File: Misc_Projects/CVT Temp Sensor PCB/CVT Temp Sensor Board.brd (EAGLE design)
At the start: 160 x 100 mm, 2 parts, among them IC1 TSD305-1SL10

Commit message: CVT Temp Board Sensor PCB
Version 1.1
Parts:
- moved IC1 27.2 mm to (99.6, 33.0)
- moved X1 24.3 mm to (81.4, 33.3), turned to 270 degrees
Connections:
- removed net N$2: X1.P$2
- removed net N$3: X1.P$3
- new net SCL: IC1.1, X1.P$3
- new net SDA: IC1.2, X1.P$2
- net +3V3: now also IC1.3
- net GND: now also IC1.4
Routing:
- net GND: track 0.00 -> 18.7 mm
- net SDA: track 0.00 -> 11.8 mm
- net SCL: track 0.00 -> 11.4 mm
- net +3V3: track 0.00 -> 9.28 mm
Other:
- board size 160 x 100 mm -> 26.9 x 24.8 mm
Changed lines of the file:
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@@
 <setting verticaltext="up"/>
 </settings>
-<grid distance="50" unitdist="mil" unit="mil" style="lines" multiple="1" display="no" altdistance="5" altunitdist="mil" altunit="mil"/>
+<grid distance="5" unitdist="mil" unit="mil" style="lines" multiple="1" display="yes" altdistance="5" altunitdist="mil" altunit="mil"/>
 <layers>
 <layer number="1" name="Top" color="4" fill="1" visible="yes" active="yes"/>
@@
 <board>
 <plain>
-<wire x1="0" y1="0" x2="160" y2="0" width="0" layer="20"/>
-<wire x1="160" y1="0" x2="160" y2="100" width="0" layer="20"/>
-<wire x1="160" y1="100" x2="0" y2="100" width="0" layer="20"/>
-<wire x1="0" y1="100" x2="0" y2="0" width="0" layer="20"/>
+<wire x1="78.867" y1="20.828" x2="105.771" y2="20.828" width="0" layer="20"/>
+<wire x1="105.771" y1="20.828" x2="105.771" y2="45.644" width="0" layer="20"/>
+<wire x1="105.771" y1="45.644" x2="78.867" y2="45.644" width="0" layer="20"/>
+<wire x1="78.867" y1="45.644" x2="78.867" y2="20.828" width="0" layer="20"/>
 </plain>
 <attributes>
@@
 </autorouter>
 <elements>
-<element name="IC1" library="TSD305-1SL10" package="TSD3051SL10" value="TSD305-1SL10" x="72.39" y="33.02" smashed="yes">
-<attribute name="DESCRIPTION" value="Board Mount Temperature Sensors TO5, I2C Interrface 0 C to +300 C" x="90.17" y="26.67" size="1.778" layer="27" display="off"/>
-<attribute name="HEIGHT" value="8.65mm" x="90.17" y="26.67" size="1.778" layer="27" display="off"/>
-<attribute name="MANUFACTURER_NAME" value="TE Connectivity" x="90.17" y="26.67" size="1.778" layer="27" display="off"/>
-<attribute name="MANUFACTURER_PART_NUMBER" value="TSD305-1SL10" x="90.17" y="26.67" size="1.778" layer="27" display="off"/>
-<attribute name="MOUSER_PART_NUMBER" value="824-TSD305-1SL10" x="90.17" y="26.67" size="1.778" layer="27" display="off"/>
-<attribute name="MOUSER_PRICE-STOCK" value="https://www.mouser.co.uk/ProductDetail/Measurement-Specialties/TSD305-1SL10?qs=l7cgNqFNU1hQbECGfV0ZYg%3D%3D" x="90.17" y="26.67" size="1.778" layer="27" display="off"/>
-<attribute name="NAME" x="69.85" y="33.02" size="1.27" layer="25" align="center"/>
-<attribute name="VALUE" x="69.85" y="40.64" size="1.27" layer="27" align="center"/>
+<element name="IC1" library="TSD305-1SL10" package="TSD3051SL10" value="TSD305-1SL10" x="99.568" y="33.02" smashed="yes">
+<attribute name="DESCRIPTION" value="Board Mount Temperature Sensors TO5, I2C Interrface 0 C to +300 C" x="117.348" y="26.67" size="1.778" layer="27" display="off"/>
+<attribute name="HEIGHT" value="8.65mm" x="117.348" y="26.67" size="1.778" layer="27" display="off"/>
+<attribute name="MANUFACTURER_NAME" value="TE Connectivity" x="117.348" y="26.67" size="1.778" layer="27" display="off"/>
+<attribute name="MANUFACTURER_PART_NUMBER" value="TSD305-1SL10" x="117.348" y="26.67" size="1.778" layer="27" display="off"/>
+<attribute name="MOUSER_PART_NUMBER" value="824-TSD305-1SL10" x="117.348" y="26.67" size="1.778" layer="27" display="off"/>
+<attribute name="MOUSER_PRICE-STOCK" value="https://www.mouser.co.uk/ProductDetail/Measurement-Specialties/TSD305-1SL10?qs=l7cgNqFNU1hQbECGfV0ZYg%3D%3D" x="117.348" y="26.67" size="1.778" layer="27" display="off"/>
+<attribute name="NAME" x="97.028" y="33.02" size="1.27" layer="25" rot="R180" align="center"/>
+<attribute name="VALUE" x="97.409" y="40.005" size="1.27" layer="27" align="center"/>
 </element>
-<element name="X1" library="GTOR - Microfit Connector" package="43045-0400" value="" x="57.15" y="33.02" smashed="yes">
-<attribute name="MATERIAL" value="" x="57.15" y="33.02" size="1.778" layer="27" display="off"/>
+<element name="X1" library="GTOR - Microfit Connector" package="43045-0400" value="" x="81.407" y="33.274" smashed="yes" rot="R270">
+<attribute name="MATERIAL" value="" x="81.407" y="33.274" size="1.778" layer="27" rot="R270" display="off"/>
 </element>
 </elements>
@@
 <signal name="+3V3">
 <contactref element="X1" pad="P$1"/>
+<contactref element="IC1" pad="3"/>
+<wire x1="85.727" y1="31.774" x2="87.32183125" y2="31.774" width="0.1524" layer="1"/>
+<wire x1="87.32183125" y1="31.774" x2="88.31543125" y2="32.7676" width="0.1524" layer="1"/>
+<wire x1="94.2356" y1="32.7676" x2="94.488" y2="33.02" width="0.1524" layer="1"/>
+<wire x1="88.31543125" y1="32.7676" x2="94.2356" y2="32.7676" width="0.1524" layer="1"/>
 </signal>
-<signal name="N$2">
+<signal name="SDA">
 <contactref element="X1" pad="P$2"/>
+<contactref element="IC1" pad="2"/>
+<wire x1="85.727" y1="34.774" x2="86.767" y2="35.814" width="0.1524" layer="1"/>
+<wire x1="96.774" y1="35.814" x2="86.767" y2="35.814" width="0.1524" layer="1"/>
+<wire x1="96.774" y1="35.814" x2="97.028" y2="35.56" width="0.1524" layer="1"/>
 </signal>
-<signal name="N$3">
+<signal name="SCL">
 <contactref element="X1" pad="P$3"/>
+<contactref element="IC1" pad="1"/>
+<wire x1="88.727" y1="31.774" x2="98.322" y2="31.774" width="0.1524" layer="1"/>
+<wire x1="98.322" y1="31.774" x2="99.568" y2="33.02" width="0.1524" layer="1"/>
 </signal>
 <signal name="GND">
 <contactref element="X1" pad="P$4"/>
+<contactref element="IC1" pad="4"/>
+<wire x1="88.727" y1="34.774" x2="99.465" y2="34.774" width="0.1524" layer="1"/>
+<wire x1="99.465" y1="34.774" x2="101.092" y2="33.147" width="0.1524" layer="1"/>
+<wire x1="101.092" y1="33.147" x2="101.092" y2="32.258" width="0.1524" layer="1"/>
+<wire x1="101.092" y1="32.258" x2="99.314" y2="30.48" width="0.1524" layer="1"/>
+<wire x1="99.314" y1="30.48" x2="97.028" y2="30.48" width="0.1524" layer="1"/>
 </signal>
 </signals>

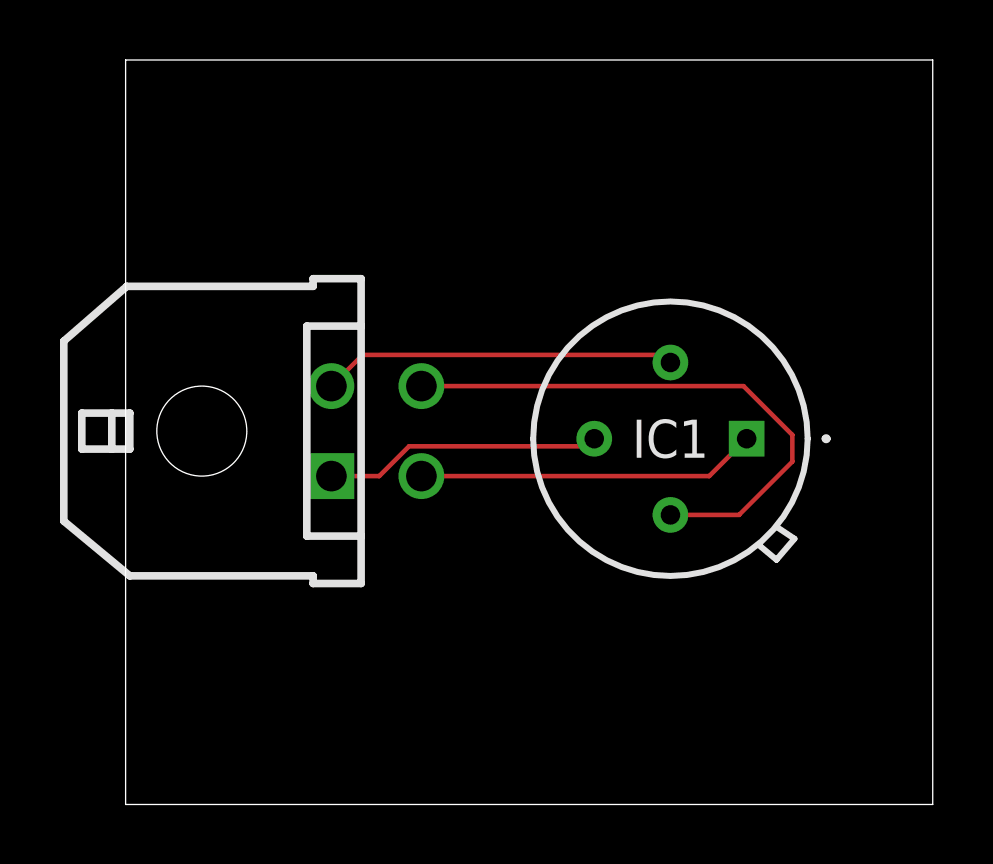
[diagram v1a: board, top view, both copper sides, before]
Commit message: added designer names
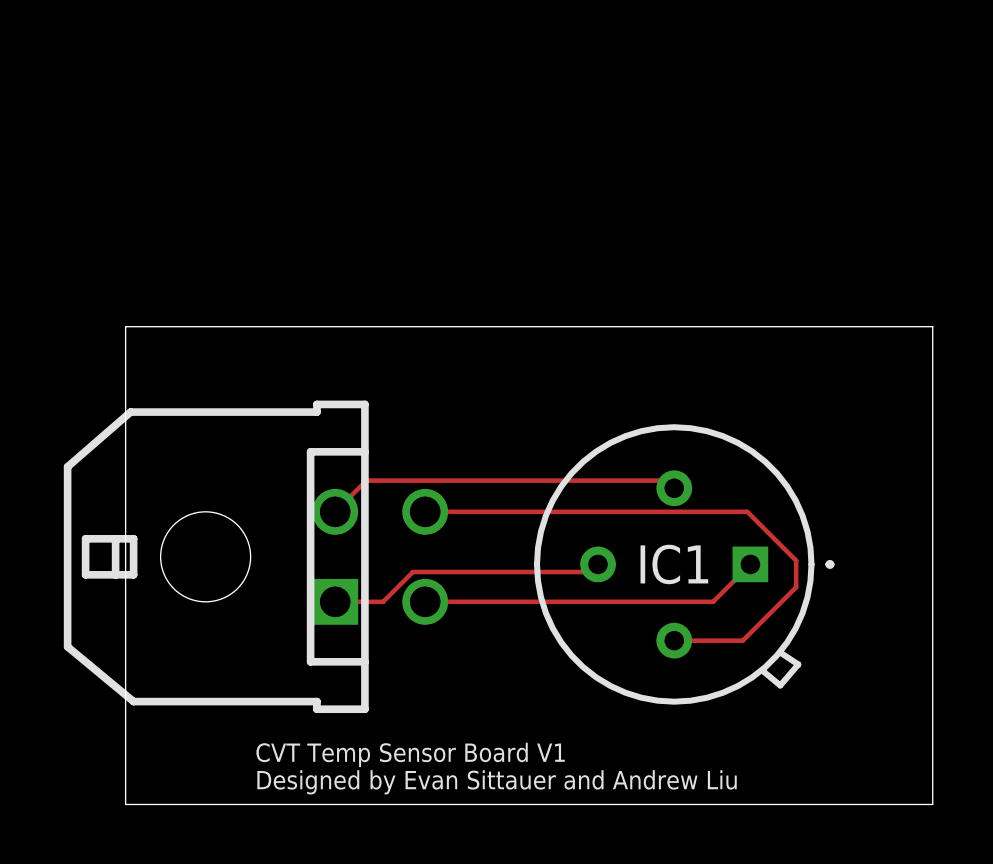
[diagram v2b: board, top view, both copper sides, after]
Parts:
- moved X1 4.19 mm to (81.5, 29.1)
- moved IC1 4.19 mm to (99.7, 28.8)
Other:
- board size 26.9 x 24.8 mm -> 26.9 x 15.9 mm
- board text added: "CVT Temp Sensor Board V1 Designed by Evan Sittauer and Andrew Liu"
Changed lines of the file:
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@@
 <layer number="43" name="vRestrict" color="2" fill="10" visible="yes" active="yes"/>
 <layer number="44" name="Drills" color="7" fill="1" visible="no" active="yes"/>
-<layer number="45" name="Holes" color="7" fill="1" visible="no" active="yes"/>
+<layer number="45" name="Holes" color="7" fill="1" visible="yes" active="yes"/>
 <layer number="46" name="Milling" color="3" fill="1" visible="no" active="yes"/>
 <layer number="47" name="Measures" color="7" fill="1" visible="no" active="yes"/>
@@
 <plain>
 <wire x1="78.867" y1="20.828" x2="105.771" y2="20.828" width="0" layer="20"/>
-<wire x1="105.771" y1="20.828" x2="105.771" y2="45.644" width="0" layer="20"/>
-<wire x1="105.771" y1="45.644" x2="78.867" y2="45.644" width="0" layer="20"/>
-<wire x1="78.867" y1="45.644" x2="78.867" y2="20.828" width="0" layer="20"/>
+<wire x1="105.771" y1="20.828" x2="105.771" y2="36.754" width="0" layer="20"/>
+<wire x1="105.771" y1="36.754" x2="78.867" y2="36.754" width="0" layer="20"/>
+<wire x1="78.867" y1="36.754" x2="78.867" y2="20.828" width="0" layer="20"/>
+<text x="83.185" y="21.336" size="0.6096" layer="25">CVT Temp Sensor Board V1
+Designed by Evan Sittauer and Andrew Liu</text>
 </plain>
 <attributes>
@@
 </autorouter>
 <elements>
-<element name="IC1" library="TSD305-1SL10" package="TSD3051SL10" value="TSD305-1SL10" x="99.568" y="33.02" smashed="yes">
-<attribute name="DESCRIPTION" value="Board Mount Temperature Sensors TO5, I2C Interrface 0 C to +300 C" x="117.348" y="26.67" size="1.778" layer="27" display="off"/>
-<attribute name="HEIGHT" value="8.65mm" x="117.348" y="26.67" size="1.778" layer="27" display="off"/>
-<attribute name="MANUFACTURER_NAME" value="TE Connectivity" x="117.348" y="26.67" size="1.778" layer="27" display="off"/>
-<attribute name="MANUFACTURER_PART_NUMBER" value="TSD305-1SL10" x="117.348" y="26.67" size="1.778" layer="27" display="off"/>
-<attribute name="MOUSER_PART_NUMBER" value="824-TSD305-1SL10" x="117.348" y="26.67" size="1.778" layer="27" display="off"/>
-<attribute name="MOUSER_PRICE-STOCK" value="https://www.mouser.co.uk/ProductDetail/Measurement-Specialties/TSD305-1SL10?qs=l7cgNqFNU1hQbECGfV0ZYg%3D%3D" x="117.348" y="26.67" size="1.778" layer="27" display="off"/>
-<attribute name="NAME" x="97.028" y="33.02" size="1.27" layer="25" rot="R180" align="center"/>
-<attribute name="VALUE" x="97.409" y="40.005" size="1.27" layer="27" align="center"/>
+<element name="IC1" library="TSD305-1SL10" package="TSD3051SL10" value="TSD305-1SL10" x="99.695" y="28.829" smashed="yes">
+<attribute name="DESCRIPTION" value="Board Mount Temperature Sensors TO5, I2C Interrface 0 C to +300 C" x="117.475" y="22.479" size="1.778" layer="27" display="off"/>
+<attribute name="HEIGHT" value="8.65mm" x="117.475" y="22.479" size="1.778" layer="27" display="off"/>
+<attribute name="MANUFACTURER_NAME" value="TE Connectivity" x="117.475" y="22.479" size="1.778" layer="27" display="off"/>
+<attribute name="MANUFACTURER_PART_NUMBER" value="TSD305-1SL10" x="117.475" y="22.479" size="1.778" layer="27" display="off"/>
+<attribute name="MOUSER_PART_NUMBER" value="824-TSD305-1SL10" x="117.475" y="22.479" size="1.778" layer="27" display="off"/>
+<attribute name="MOUSER_PRICE-STOCK" value="https://www.mouser.co.uk/ProductDetail/Measurement-Specialties/TSD305-1SL10?qs=l7cgNqFNU1hQbECGfV0ZYg%3D%3D" x="117.475" y="22.479" size="1.778" layer="27" display="off"/>
+<attribute name="NAME" x="97.155" y="28.829" size="1.27" layer="25" rot="R180" align="center"/>
+<attribute name="VALUE" x="97.536" y="35.814" size="1.27" layer="27" align="center"/>
 </element>
-<element name="X1" library="GTOR - Microfit Connector" package="43045-0400" value="" x="81.407" y="33.274" smashed="yes" rot="R270">
-<attribute name="MATERIAL" value="" x="81.407" y="33.274" size="1.778" layer="27" rot="R270" display="off"/>
+<element name="X1" library="GTOR - Microfit Connector" package="43045-0400" value="" x="81.534" y="29.083" smashed="yes" rot="R270">
+<attribute name="MATERIAL" value="" x="81.534" y="29.083" size="1.778" layer="27" rot="R270" display="off"/>
 </element>
 </elements>
@@
 <contactref element="X1" pad="P$1"/>
 <contactref element="IC1" pad="3"/>
-<wire x1="85.727" y1="31.774" x2="87.32183125" y2="31.774" width="0.1524" layer="1"/>
-<wire x1="87.32183125" y1="31.774" x2="88.31543125" y2="32.7676" width="0.1524" layer="1"/>
-<wire x1="94.2356" y1="32.7676" x2="94.488" y2="33.02" width="0.1524" layer="1"/>
-<wire x1="88.31543125" y1="32.7676" x2="94.2356" y2="32.7676" width="0.1524" layer="1"/>
+<wire x1="85.854" y1="27.583" x2="87.44883125" y2="27.583" width="0.1524" layer="1"/>
+<wire x1="87.44883125" y1="27.583" x2="88.44243125" y2="28.5766" width="0.1524" layer="1"/>
+<wire x1="94.3626" y1="28.5766" x2="94.615" y2="28.829" width="0.1524" layer="1"/>
+<wire x1="88.44243125" y1="28.5766" x2="94.3626" y2="28.5766" width="0.1524" layer="1"/>
 </signal>
 <signal name="SDA">
 <contactref element="X1" pad="P$2"/>
 <contactref element="IC1" pad="2"/>
-<wire x1="85.727" y1="34.774" x2="86.767" y2="35.814" width="0.1524" layer="1"/>
-<wire x1="96.774" y1="35.814" x2="86.767" y2="35.814" width="0.1524" layer="1"/>
-<wire x1="96.774" y1="35.814" x2="97.028" y2="35.56" width="0.1524" layer="1"/>
+<wire x1="85.854" y1="30.583" x2="86.894" y2="31.623" width="0.1524" layer="1"/>
+<wire x1="96.901" y1="31.623" x2="86.894" y2="31.623" width="0.1524" layer="1"/>
+<wire x1="96.901" y1="31.623" x2="97.155" y2="31.369" width="0.1524" layer="1"/>
 </signal>
 <signal name="SCL">
 <contactref element="X1" pad="P$3"/>
 <contactref element="IC1" pad="1"/>
-<wire x1="88.727" y1="31.774" x2="98.322" y2="31.774" width="0.1524" layer="1"/>
-<wire x1="98.322" y1="31.774" x2="99.568" y2="33.02" width="0.1524" layer="1"/>
+<wire x1="88.854" y1="27.583" x2="98.449" y2="27.583" width="0.1524" layer="1"/>
+<wire x1="98.449" y1="27.583" x2="99.695" y2="28.829" width="0.1524" layer="1"/>
 </signal>
 <signal name="GND">
 <contactref element="X1" pad="P$4"/>
 <contactref element="IC1" pad="4"/>
-<wire x1="88.727" y1="34.774" x2="99.465" y2="34.774" width="0.1524" layer="1"/>
-<wire x1="99.465" y1="34.774" x2="101.092" y2="33.147" width="0.1524" layer="1"/>
-<wire x1="101.092" y1="33.147" x2="101.092" y2="32.258" width="0.1524" layer="1"/>
-<wire x1="101.092" y1="32.258" x2="99.314" y2="30.48" width="0.1524" layer="1"/>
-<wire x1="99.314" y1="30.48" x2="97.028" y2="30.48" width="0.1524" layer="1"/>
+<wire x1="88.854" y1="30.583" x2="99.592" y2="30.583" width="0.1524" layer="1"/>
+<wire x1="99.592" y1="30.583" x2="101.219" y2="28.956" width="0.1524" layer="1"/>
+<wire x1="101.219" y1="28.956" x2="101.219" y2="28.067" width="0.1524" layer="1"/>
+<wire x1="101.219" y1="28.067" x2="99.441" y2="26.289" width="0.1524" layer="1"/>
+<wire x1="99.441" y1="26.289" x2="97.155" y2="26.289" width="0.1524" layer="1"/>
 </signal>
 </signals>
@@
 </board>
 </drawing>
+<compatibility>
+<note version="6.3" minversion="6.2.2" severity="warning">
+Since Version 6.2.2 text objects can contain more than one line,
+which will not be processed correctly with this version.
+</note>
+</compatibility>
 </eagle>
